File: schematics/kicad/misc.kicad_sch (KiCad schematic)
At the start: 0 parts

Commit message: Populate misc page with P4 connector and caps Finish MUX, RAM and most of Output Lots of progress on Control Lay out root and connect most components
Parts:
- added C1, C10, C11, C12, C13, C14, C15, C16, C17, C18, C19, C2, C20, C21, C22, C23, C24, C25, C26, C27, C28, C29, C3, C30, C31, C32, C33, C34, C35, C36, C37, C38, C39, C4, C40, C5, C6, C7, C8, C9: 0.1uF, Capacitor_THT:C_Rect_L7.0mm_W2.0mm_P5.00mm, symbol Device:C
- added P4: DIN41612_03x32_C_Split, Connector_DIN:DIN41612_R_3x32_Male_Vertical_THT, symbol Connector:DIN41612_03x32_C_Split
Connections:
- new net A0: P4.a18 (Pin_a18)
- new net A1: P4.a19 (Pin_a19)
- new net A10: P4.a28 (Pin_a28)
- new net A11: P4.a29 (Pin_a29)
- new net A12: P4.a30 (Pin_a30)
- new net A2: P4.a20 (Pin_a20)
- new net A3: P4.a21 (Pin_a21)
- new net A4: P4.a22 (Pin_a22)
- new net A5: P4.a23 (Pin_a23)
- new net A6: P4.a24 (Pin_a24)
- new net A7: P4.a25 (Pin_a25)
- new net A8: P4.a26 (Pin_a26)
- new net A9: P4.a27 (Pin_a27)
- new net C.S3-: P4.c31 (Pin_c31)
- new net CLK: P4.b2 (Pin_b2)
- new net D0: P4.a1 (Pin_a1)
- new net D1: P4.a2 (Pin_a2)
- new net D10: P4.a11 (Pin_a11)
- new net D11: P4.a12 (Pin_a12)
- new net D12: P4.a13 (Pin_a13)
- new net D13: P4.a14 (Pin_a14)
- new net D14: P4.a15 (Pin_a15)
- new net D15: P4.a16 (Pin_a16)
- new net D16: P4.c1 (Pin_c1)
- new net D17: P4.c2 (Pin_c2)
- new net D18: P4.c3 (Pin_c3)
- new net D19: P4.c4 (Pin_c4)
- new net D2: P4.a3 (Pin_a3)
- new net D20: P4.c5 (Pin_c5)
- new net D21: P4.c6 (Pin_c6)
- new net D22: P4.c7 (Pin_c7)
- new net D23: P4.c8 (Pin_c8)
- new net D24: P4.c9 (Pin_c9)
- new net D25: P4.c10 (Pin_c10)
- new net D26: P4.c11 (Pin_c11)
- new net D27: P4.c12 (Pin_c12)
- new net D28: P4.c13 (Pin_c13)
- new net D29: P4.c14 (Pin_c14)
- new net D3: P4.a4 (Pin_a4)
- new net D30: P4.c15 (Pin_c15)
- new net D31: P4.c16 (Pin_c16)
- new net D4: P4.a5 (Pin_a5)
- new net D5: P4.a6 (Pin_a6)
- new net D6: P4.a7 (Pin_a7)
- new net D7: P4.a8 (Pin_a8)
- new net D8: P4.a9 (Pin_a9)
- new net D9: P4.a10 (Pin_a10)
- new net DISACC-: P4.b28 (Pin_b28)
- new net DSACK0-: P4.b10 (Pin_b10)
- new net DSACK1-: P4.b11 (Pin_b11)
- new net EN.VIDEO: P4.b23 (Pin_b23)
- new net GND: C1.2, C10.2, C11.2, C12.2, C13.2, C14.2, C15.2, C16.2, C17.2, C18.2, C19.2, C2.2, C20.2, C21.2, C22.2, C23.2, C24.2, C25.2, C26.2, C27.2, C28.2, C29.2, C3.2, C30.2, C31.2, C32.2, C33.2, C34.2, C35.2, C36.2, C37.2, C38.2, C39.2, C4.2, C40.2, C5.2, C6.2, C7.2, C8.2, C9.2, P4.a17 (Pin_a17), P4.b1 (Pin_b1), P4.b12 (Pin_b12), P4.b17 (Pin_b17), P4.b21 (Pin_b21), P4.b24 (Pin_b24), P4.b26 (Pin_b26), P4.b27 (Pin_b27), P4.b3 (Pin_b3), P4.b5 (Pin_b5), P4.b6 (Pin_b6), P4.b7 (Pin_b7), P4.b8 (Pin_b8), P4.b9 (Pin_b9), P4.c17 (Pin_c17), P4.c30 (Pin_c30)
- new net INIT-: P4.b30 (Pin_b30)
- new net P4AS-: P4.b25 (Pin_b25), P4.b29 (Pin_b29)
- new net PA13: P4.c18 (Pin_c18)
- new net PA14: P4.c19 (Pin_c19)
- new net PA15: P4.c20 (Pin_c20)
- new net PA16: P4.c21 (Pin_c21)
- new net PA17: P4.c22 (Pin_c22)
- new net PA18: P4.c23 (Pin_c23)
- new net PA19: P4.c24 (Pin_c24)
- new net PA20: P4.c25 (Pin_c25)
- new net PA21: P4.c26 (Pin_c26)
- new net PA22: P4.c27 (Pin_c27)
- new net PA23: P4.c28 (Pin_c28)
- new net PA24: P4.c29 (Pin_c29)
- new net SIZ0: P4.b18 (Pin_b18)
- new net SIZ1: P4.b19 (Pin_b19)
- new net V.INTY-: P4.b22 (Pin_b22)
- new net VCC: C1.1, C10.1, C11.1, C12.1, C13.1, C14.1, C15.1, C16.1, C17.1, C18.1, C19.1, C2.1, C20.1, C21.1, C22.1, C23.1, C24.1, C25.1, C26.1, C27.1, C28.1, C29.1, C3.1, C30.1, C31.1, C32.1, C33.1, C34.1, C35.1, C36.1, C37.1, C38.1, C39.1, C4.1, C40.1, C5.1, C6.1, C7.1, C8.1, C9.1, P4.a32 (Pin_a32), P4.b13 (Pin_b13), P4.b14 (Pin_b14), P4.b15 (Pin_b15), P4.b16 (Pin_b16), P4.b32 (Pin_b32), P4.c32 (Pin_c32)
- new net VEE: P4.a31 (Pin_a31), P4.b31 (Pin_b31)
- new net WRITE-: P4.b20 (Pin_b20)

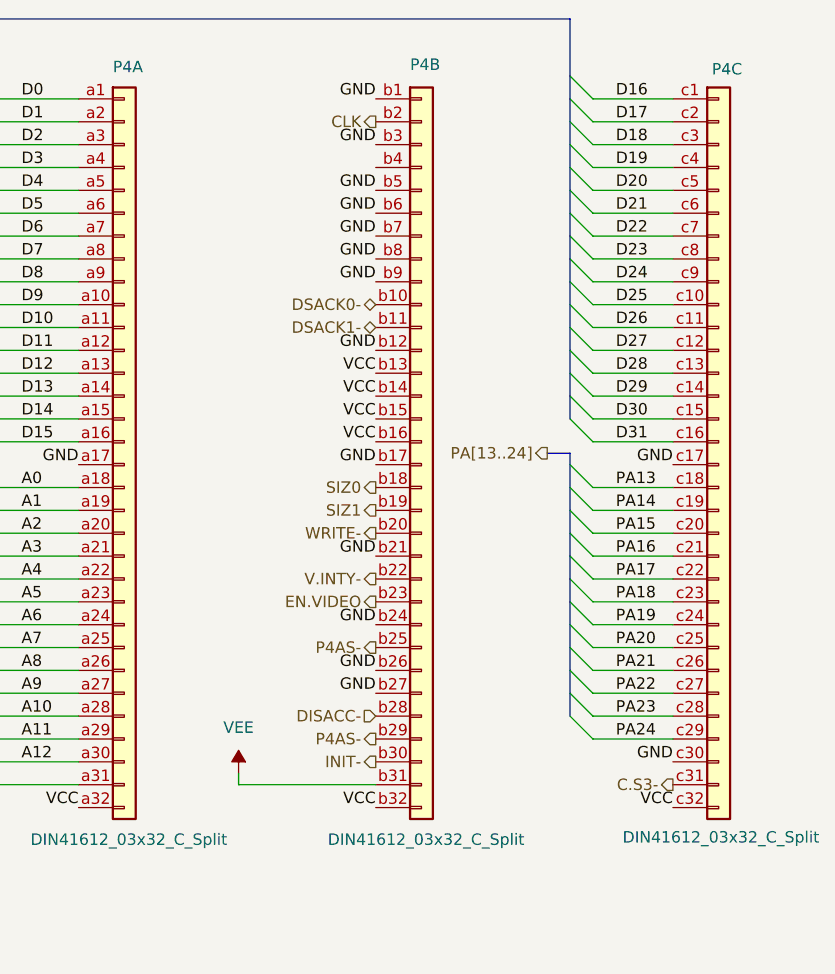
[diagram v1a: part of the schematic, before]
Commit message: Fix layout of the memory chips based on the board Fix the orientation of the P4 connector Connect CS.DAC- based on the board Change the orientation of the ECL resistors to route better Fix the copper islands to match the board, only DAC is on analog island, ECL and crystal are separate. Fix ECL VCC to VCC Confirm VEE not used Add PALs - U1000 missing
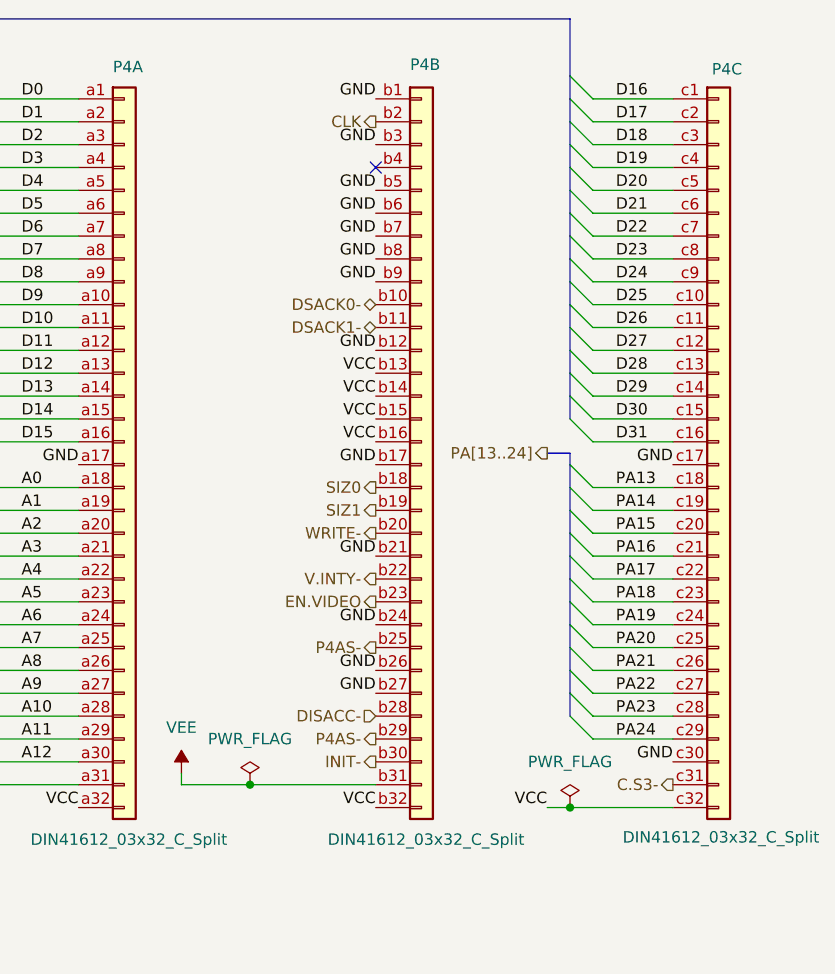
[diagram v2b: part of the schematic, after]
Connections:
- no-connect marks 0 -> 1
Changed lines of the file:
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@@
 	)
 	(junction
+		(at 195.58 121.92)
+		(diameter 0)
+		(color 0 0 0 0)
+	)
+	(junction
 		(at 31.75 91.44)
 		(diameter 0)
@@
 	)
 	(junction
+		(at 231.14 124.46)
+		(diameter 0)
+		(color 0 0 0 0)
+	)
+	(junction
 		(at 45.72 138.43)
 		(diameter 0)
@@
 		(color 0 0 0 0)
 	)
+	(no_connect
+		(at 209.55 53.34)
+	)
 	(bus_entry
 		(at 165.1 106.68)
@@
 	(wire
 		(pts
-			(xy 194.31 120.65) (xy 194.31 121.92)
+			(xy 187.96 120.65) (xy 187.96 121.92)
 		)
 		(stroke
@@
 	(wire
 		(pts
+			(xy 195.58 121.92) (xy 187.96 121.92)
+		)
+		(stroke
+			(width 0)
+			(type default)
+		)
+	)
+	(wire
+		(pts
 			(xy 167.64 60.96) (xy 176.53 60.96)
 		)
@@
 		)
 	)
-	(wire
-		(pts
-			(xy 209.55 121.92) (xy 194.31 121.92)
-		)
-		(stroke
-			(width 0)
-			(type default)
-		)
-	)
 	(bus
 		(pts
@@
 	(wire
 		(pts
+			(xy 231.14 124.46) (xy 242.57 124.46)
+		)
+		(stroke
+			(width 0)
+			(type default)
+		)
+	)
+	(wire
+		(pts
 			(xy 59.69 115.57) (xy 73.66 115.57)
 		)
@@
 		)
 	)
+	(wire
+		(pts
+			(xy 195.58 121.92) (xy 209.55 121.92)
+		)
+		(stroke
+			(width 0)
+			(type default)
+		)
+	)
 	(bus
 		(pts
@@
 		)
 	)
+	(wire
+		(pts
+			(xy 228.6 124.46) (xy 231.14 124.46)
+		)
+		(stroke
+			(width 0)
+			(type default)
+		)
+	)
 	(bus
 		(pts
@@
 	)
 	(label "VCC"
-		(at 242.57 124.46 180)
+		(at 228.6 124.46 180)
 		(effects
 			(font
@@
 	)
 	(symbol
+		(lib_id "power:PWR_FLAG")
+		(at 195.58 121.92 0)
+		(unit 1)
+		(exclude_from_sim no)
+		(in_bom yes)
+		(on_board yes)
+		(dnp no)
+		(fields_autoplaced yes)
+		(property "Reference" "#FLG02"
+			(at 195.58 120.015 0)
+			(effects
+				(font
+					(size 1.27 1.27)
+				)
+				(hide yes)
+			)
+		)
+		(property "Value" "PWR_FLAG"
+			(at 195.58 116.84 0)
+			(effects
+				(font
+					(size 1.27 1.27)
+				)
+			)
+		)
+		(property "Footprint" ""
+			(at 195.58 121.92 0)
+			(effects
+				(font
+					(size 1.27 1.27)
+				)
+				(hide yes)
+			)
+		)
+		(property "Datasheet" "~"
+			(at 195.58 121.92 0)
+			(effects
+				(font
+					(size 1.27 1.27)
+				)
+				(hide yes)
+			)
+		)
+		(property "Description" "Special symbol for telling ERC where power comes from"
+			(at 195.58 121.92 0)
+			(effects
+				(font
+					(size 1.27 1.27)
+				)
+				(hide yes)
+			)
+		)
+		(pin "1"
+		)
+		(instances
+			(project "cg4"
+				(path "/7c2b6a13-c303-4adb-8eed-6e6a9ac5307e/1e4cb93f-b1a2-43f5-bc06-3785820075fb"
+					(reference "#FLG02")
+					(unit 1)
+				)
+			)
+		)
+	)
+	(symbol
 		(lib_id "Device:C")
 		(at 45.72 134.62 0)
@@
 	)
 	(symbol
+		(lib_id "power:PWR_FLAG")
+		(at 231.14 124.46 0)
+		(unit 1)
+		(exclude_from_sim no)
+		(in_bom yes)
+		(on_board yes)
+		(dnp no)
+		(fields_autoplaced yes)
+		(property "Reference" "#FLG01"
+			(at 231.14 122.555 0)
+			(effects
+				(font
+					(size 1.27 1.27)
+				)
+				(hide yes)
+			)
+		)
+		(property "Value" "PWR_FLAG"
+			(at 231.14 119.38 0)
+			(effects
+				(font
+					(size 1.27 1.27)
+				)
+			)
+		)
+		(property "Footprint" ""
+			(at 231.14 124.46 0)
+			(effects
+				(font
+					(size 1.27 1.27)
+				)
+				(hide yes)
+			)
+		)
+		(property "Datasheet" "~"
+			(at 231.14 124.46 0)
+			(effects
+				(font
+					(size 1.27 1.27)
+				)
+				(hide yes)
+			)
+		)
+		(property "Description" "Special symbol for telling ERC where power comes from"
+			(at 231.14 124.46 0)
+			(effects
+				(font
+					(size 1.27 1.27)
+				)
+				(hide yes)
+			)
+		)
+		(pin "1"
+		)
+		(instances
+			(project ""
+				(path "/7c2b6a13-c303-4adb-8eed-6e6a9ac5307e/1e4cb93f-b1a2-43f5-bc06-3785820075fb"
+					(reference "#FLG01")
+					(unit 1)
+				)
+			)
+		)
+	)
+	(symbol
 		(lib_id "power:VCC")
 		(at 24.13 107.95 0)
@@
 	(symbol
 		(lib_id "power:VEE")
-		(at 194.31 120.65 0)
+		(at 187.96 120.65 0)
 		(unit 1)
 		(exclude_from_sim no)
@@
 		(fields_autoplaced yes)
 		(property "Reference" "#PWR016"
-			(at 194.31 124.46 0)
+			(at 187.96 124.46 0)
 			(effects
 				(font
@@
 		)
 		(property "Value" "VEE"
-			(at 194.31 115.57 0)
+			(at 187.96 115.57 0)
 			(effects
 				(font
@@
 		)
 		(property "Footprint" ""
-			(at 194.31 120.65 0)
+			(at 187.96 120.65 0)
 			(effects
 				(font
@@
 		)
 		(property "Datasheet" ""
-			(at 194.31 120.65 0)
+			(at 187.96 120.65 0)
 			(effects
 				(font
@@
 		)
 		(property "Description" "Power symbol creates a global label with name \"VEE\""
-			(at 194.31 120.65 0)
+			(at 187.96 120.65 0)
 			(effects
 				(font

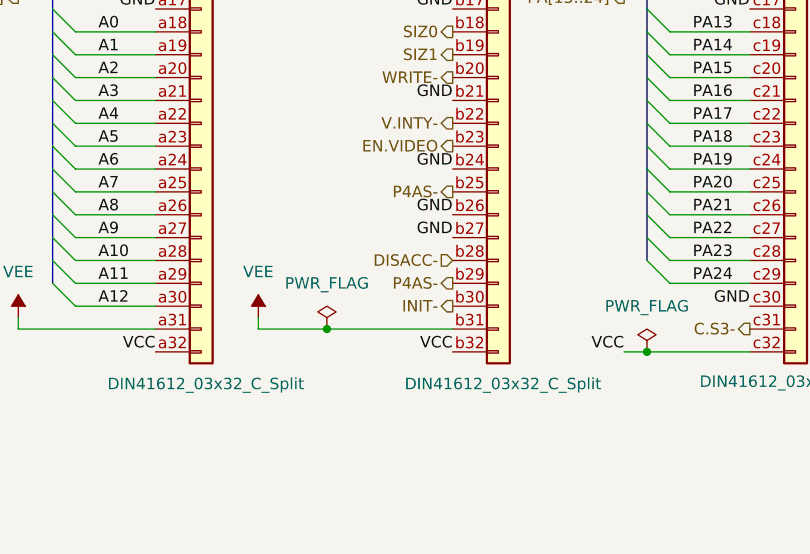
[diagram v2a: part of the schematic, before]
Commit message: Fix the schematics as per the tracing of the actual board. fork a layout with the original positioning. New version PCB that should make routing easier.
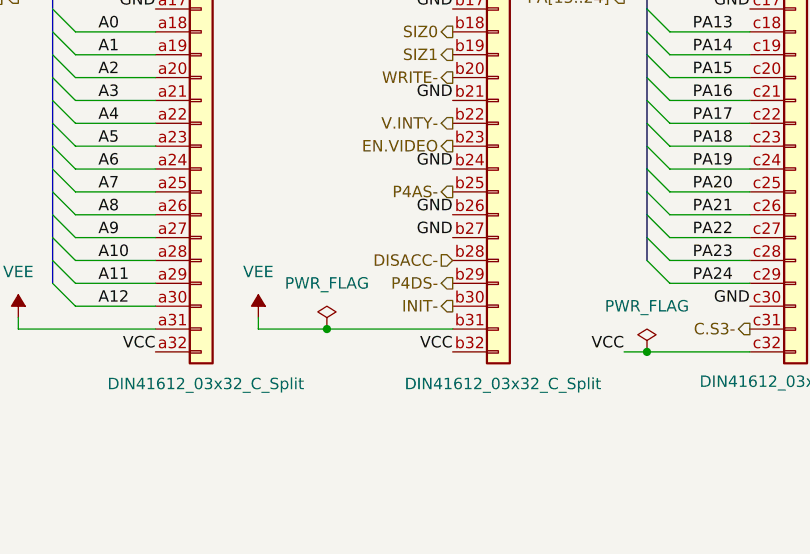
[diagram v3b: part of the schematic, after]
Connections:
- net P4AS-: no longer P4.b29 (Pin_b29)
- new net P4DS-: P4.b29 (Pin_b29)
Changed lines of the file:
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@@
 		)
 	)
-	(hierarchical_label "P4AS-"
+	(hierarchical_label "P4DS-"
 		(shape output)
 		(at 209.55 116.84 180)

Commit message: Finish routing and misc fixes in the analog section
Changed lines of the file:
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@@
 	)
 	(junction
+		(at 208.28 45.72)
+		(diameter 0)
+		(color 0 0 0 0)
+	)
+	(junction
 		(at 73.66 38.1)
 		(diameter 0)
@@
 	(wire
 		(pts
+			(xy 207.01 45.72) (xy 208.28 45.72)
+		)
+		(stroke
+			(width 0)
+			(type default)
+		)
+	)
+	(wire
+		(pts
 			(xy 233.68 63.5) (xy 242.57 63.5)
 		)
@@
 	(wire
 		(pts
+			(xy 208.28 45.72) (xy 209.55 45.72)
+		)
+		(stroke
+			(width 0)
+			(type default)
+		)
+	)
+	(wire
+		(pts
 			(xy 233.68 71.12) (xy 242.57 71.12)
 		)
@@
 	)
 	(label "GND"
-		(at 209.55 45.72 180)
+		(at 207.01 45.72 180)
 		(effects
 			(font
@@
 					(unit 1)
 				)
+			)
+		)
+	)
+	(symbol
+		(lib_id "power:PWR_FLAG")
+		(at 208.28 45.72 0)
+		(unit 1)
+		(exclude_from_sim no)
+		(in_bom yes)
+		(on_board yes)
+		(dnp no)
+		(fields_autoplaced yes)
+		(property "Reference" "#FLG05"
+			(at 208.28 43.815 0)
+			(effects
+				(font
+					(size 1.27 1.27)
+				)
+				(hide yes)
+			)
+		)
+		(property "Value" "PWR_FLAG"
+			(at 208.28 40.64 0)
+			(effects
+				(font
+					(size 1.27 1.27)
+				)
+			)
+		)
+		(property "Footprint" ""
+			(at 208.28 45.72 0)
+			(effects
+				(font
+					(size 1.27 1.27)
+				)
+				(hide yes)
+			)
+		)
+		(property "Datasheet" "~"
+			(at 208.28 45.72 0)
+			(effects
+				(font
+					(size 1.27 1.27)
+				)
+				(hide yes)
+			)
+		)
+		(property "Description" "Special symbol for telling ERC where power comes from"
+			(at 208.28 45.72 0)
+			(effects
+				(font
+					(size 1.27 1.27)
+				)
+				(hide yes)
+			)
+		)
+		(pin "1"
+		)
+		(instances
+			(project "cg4"
+				(path "/7c2b6a13-c303-4adb-8eed-6e6a9ac5307e/1e4cb93f-b1a2-43f5-bc06-3785820075fb"
+					(reference "#FLG05")
+					(unit 1)
+				)
